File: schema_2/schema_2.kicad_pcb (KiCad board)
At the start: 2 copper layers, 241 x 211 mm, 377 parts, among them J1 USB_C_Receptacle_PowerOnly_6P, J2 Conn_01x03_Pin, J3 Conn_01x04_Pin, SW103 SW_Push, SW104 SW_Push, SW105 SW_Push, SW21 SK12D07VG3, SW92 SK12D07VG3, U1 AP2112K-3.3, U2 W25Q128JVS, U3 74AHCT125, U4 STM32G070RBTx, U5 MAX98357A, U6 WEMOS_D1_mini, Y1 SX3M8.000M20F30TNN

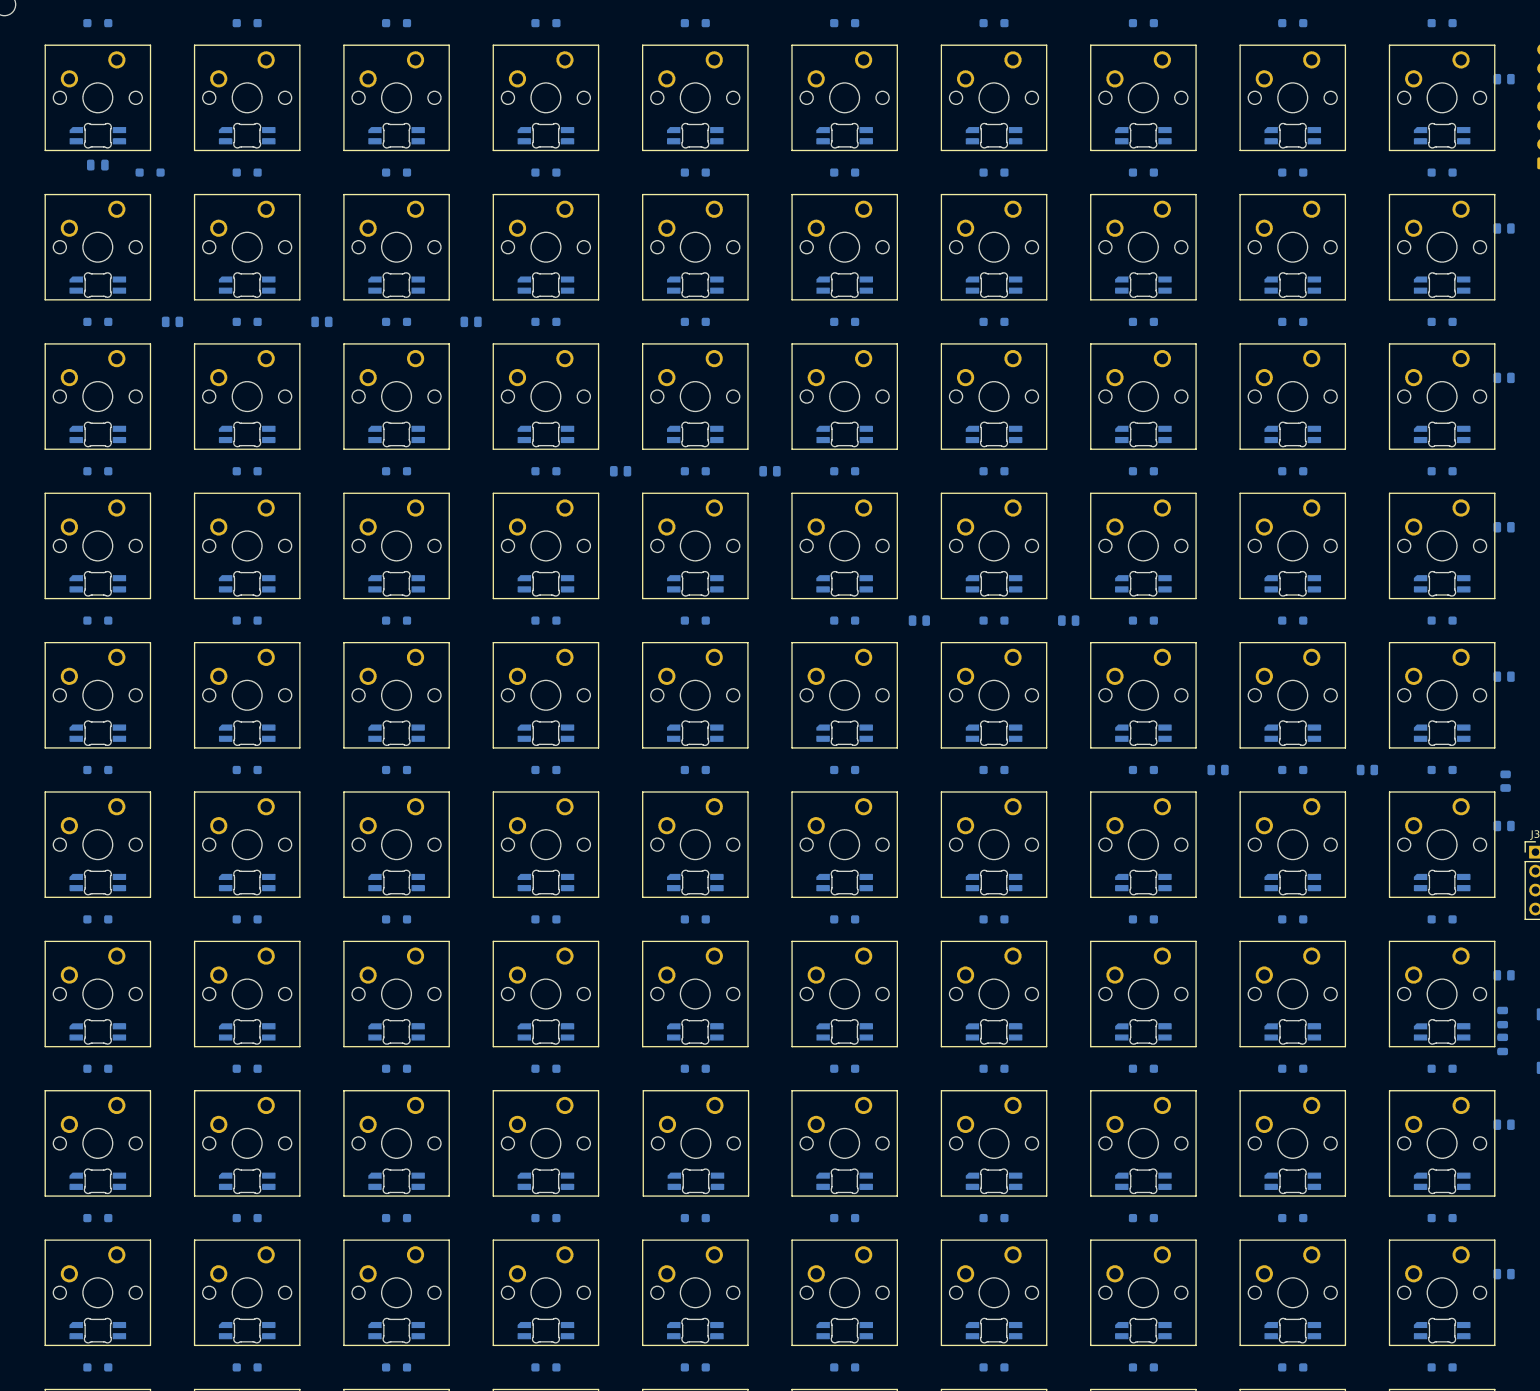
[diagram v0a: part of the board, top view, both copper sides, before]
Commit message: Update schematic and pcb with new snake connection
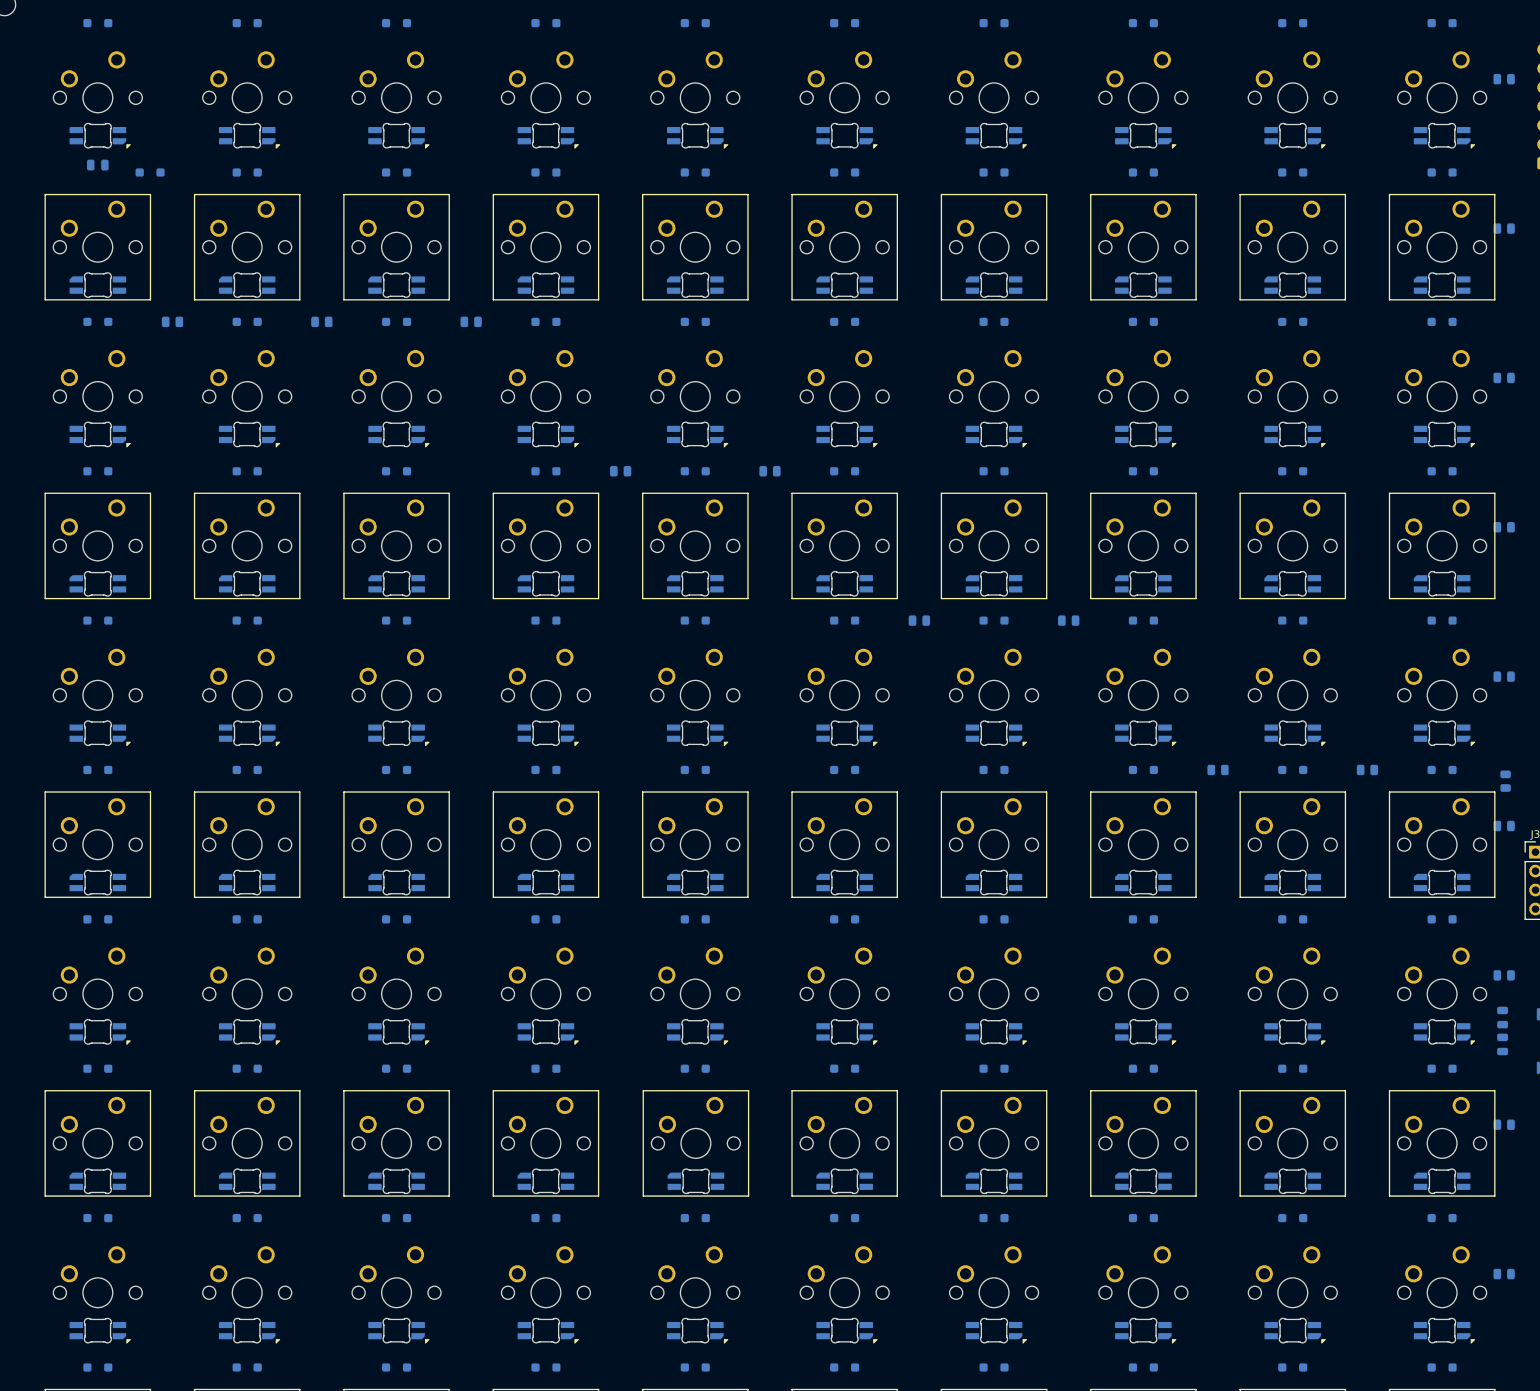
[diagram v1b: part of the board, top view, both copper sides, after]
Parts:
- SW1, SW10, SW2, SW22, SW23, SW24, SW25, SW26, SW27, SW28, SW29, SW3, SW30, SW31, SW4, SW42, SW43, SW44, SW45, SW46, SW47, SW48, SW49, SW5, SW50, SW51, SW6, SW62, SW63, SW64, SW65, SW66, SW67, SW68, SW69, SW7, SW70, SW71, SW8, SW82, SW83, SW84, SW85, SW86, SW87, SW88, SW89, SW9, SW90, SW91: footprint sw_led:SW_MX_1u_SK6812MINI-E_ROTATE -> sw_led:SW_MX_1u_SK6812MINI-E
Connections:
- net Net-(SW100-DIN) renamed /led_97
- net Net-(SW100-DOUT) renamed /led_98
- net Net-(SW101-DOUT) renamed /led_99
- net Net-(SW11-DOUT) renamed /led_11
- net Net-(SW12-DOUT) renamed /led_12
- net Net-(SW13-DOUT) renamed /led_13
- net Net-(SW14-DOUT) renamed /led_14
- net Net-(SW15-DOUT) renamed /led_15
- net Net-(SW16-DOUT) renamed /led_16
- net Net-(SW17-DOUT) renamed /led_17
- net Net-(SW18-DOUT) renamed /led_18
- net Net-(SW19-DOUT) renamed /led_19
- net Net-(SW32-DOUT) renamed /led_31
- net Net-(SW33-DOUT) renamed /led_32
- net Net-(SW34-DOUT) renamed /led_33
- net Net-(SW35-DOUT) renamed /led_34
- net Net-(SW36-DOUT) renamed /led_35
- net Net-(SW37-DOUT) renamed /led_36
- net Net-(SW38-DOUT) renamed /led_37
- net Net-(SW39-DOUT) renamed /led_38
- net Net-(SW40-DOUT) renamed /led_39
- net Net-(SW52-DOUT) renamed /led_51
- net Net-(SW53-DOUT) renamed /led_52
- net Net-(SW54-DOUT) renamed /led_53
- net Net-(SW55-DOUT) renamed /led_54
- net Net-(SW56-DOUT) renamed /led_55
- net Net-(SW57-DOUT) renamed /led_56
- net Net-(SW58-DOUT) renamed /led_57
- net Net-(SW59-DOUT) renamed /led_58
- net Net-(SW60-DOUT) renamed /led_59
- net Net-(SW72-DOUT) renamed /led_71
- net Net-(SW73-DOUT) renamed /led_72
- net Net-(SW74-DOUT) renamed /led_73
- net Net-(SW75-DOUT) renamed /led_74
- net Net-(SW76-DOUT) renamed /led_75
- net Net-(SW77-DOUT) renamed /led_76
- net Net-(SW78-DOUT) renamed /led_77
- net Net-(SW79-DOUT) renamed /led_78
- net Net-(SW80-DOUT) renamed /led_79
- net Net-(SW93-DOUT) renamed /led_91
- net Net-(SW94-DOUT) renamed /led_92
- net Net-(SW95-DOUT) renamed /led_93
- net Net-(SW96-DOUT) renamed /led_94
- net Net-(SW97-DOUT) renamed /led_95
- net Net-(SW98-DOUT) renamed /led_96
- SW1 pad 2: Net-(SW1-DOUT) -> /led_10
- SW1 pad 4: /rgb_data_5V -> /led_9
- SW10 pad 2: /led_out_1 -> /led_1
- SW10 pad 4: Net-(SW10-DIN) -> /rgb_data_5V
- SW11 pad 4: /led_out_1 -> /led_10
- SW2 pad 2: Net-(SW2-DOUT) -> /led_9
- SW2 pad 4: Net-(SW1-DOUT) -> /led_8
- SW20 pad 2: /led_out_2 -> /led_20
- SW22 pad 2: Net-(SW22-DOUT) -> /led_30
- SW22 pad 4: /led_out_2 -> /led_29
- SW23 pad 2: Net-(SW23-DOUT) -> /led_29
- SW23 pad 4: Net-(SW22-DOUT) -> /led_28
- SW24 pad 2: Net-(SW24-DOUT) -> /led_28
- SW24 pad 4: Net-(SW23-DOUT) -> /led_27
- SW25 pad 2: Net-(SW25-DOUT) -> /led_27
- SW25 pad 4: Net-(SW24-DOUT) -> /led_26
- SW26 pad 2: Net-(SW26-DOUT) -> /led_26
- SW26 pad 4: Net-(SW25-DOUT) -> /led_25
- SW27 pad 2: Net-(SW27-DOUT) -> /led_25
- SW27 pad 4: Net-(SW26-DOUT) -> /led_24
- SW28 pad 2: Net-(SW28-DOUT) -> /led_24
- SW28 pad 4: Net-(SW27-DOUT) -> /led_23
- SW29 pad 2: Net-(SW29-DOUT) -> /led_23
- SW29 pad 4: Net-(SW28-DOUT) -> /led_22
- SW3 pad 2: Net-(SW3-DOUT) -> /led_8
- SW3 pad 4: Net-(SW2-DOUT) -> /led_7
- SW30 pad 2: Net-(SW30-DOUT) -> /led_22
- SW30 pad 4: Net-(SW29-DOUT) -> /led_21
- SW31 pad 2: /led_out_3 -> /led_21
- SW31 pad 4: Net-(SW30-DOUT) -> /led_20
- SW32 pad 4: /led_out_3 -> /led_30
- SW4 pad 2: Net-(SW4-DOUT) -> /led_7
- SW4 pad 4: Net-(SW3-DOUT) -> /led_6
- SW41 pad 2: /led_out_4 -> /led_40
- SW42 pad 2: Net-(SW42-DOUT) -> /led_50
- SW42 pad 4: /led_out_4 -> /led_49
- SW43 pad 2: Net-(SW43-DOUT) -> /led_49
- SW43 pad 4: Net-(SW42-DOUT) -> /led_48
- SW44 pad 2: Net-(SW44-DOUT) -> /led_48
- SW44 pad 4: Net-(SW43-DOUT) -> /led_47
- SW45 pad 2: Net-(SW45-DOUT) -> /led_47
- SW45 pad 4: Net-(SW44-DOUT) -> /led_46
- SW46 pad 2: Net-(SW46-DOUT) -> /led_46
- SW46 pad 4: Net-(SW45-DOUT) -> /led_45
- SW47 pad 2: Net-(SW47-DOUT) -> /led_45
- SW47 pad 4: Net-(SW46-DOUT) -> /led_44
- SW48 pad 2: Net-(SW48-DOUT) -> /led_44
- SW48 pad 4: Net-(SW47-DOUT) -> /led_43
- SW49 pad 2: Net-(SW49-DOUT) -> /led_43
- SW49 pad 4: Net-(SW48-DOUT) -> /led_42
- SW5 pad 2: Net-(SW5-DOUT) -> /led_6
- SW5 pad 4: Net-(SW4-DOUT) -> /led_5
- SW50 pad 2: Net-(SW50-DOUT) -> /led_42
- SW50 pad 4: Net-(SW49-DOUT) -> /led_41
- SW51 pad 2: /led_out_5 -> /led_41
- SW51 pad 4: Net-(SW50-DOUT) -> /led_40
- SW52 pad 4: /led_out_5 -> /led_50
- SW6 pad 2: Net-(SW6-DOUT) -> /led_5
- SW6 pad 4: Net-(SW5-DOUT) -> /led_4
- SW61 pad 2: /led_out_6 -> /led_60
- SW62 pad 2: Net-(SW62-DOUT) -> /led_70
- SW62 pad 4: /led_out_6 -> /led_69
- SW63 pad 2: Net-(SW63-DOUT) -> /led_69
- SW63 pad 4: Net-(SW62-DOUT) -> /led_68
- SW64 pad 2: Net-(SW64-DOUT) -> /led_68
- SW64 pad 4: Net-(SW63-DOUT) -> /led_67
- SW65 pad 2: Net-(SW65-DOUT) -> /led_67
- SW65 pad 4: Net-(SW64-DOUT) -> /led_66
- SW66 pad 2: Net-(SW66-DOUT) -> /led_66
- SW66 pad 4: Net-(SW65-DOUT) -> /led_65
- SW67 pad 2: Net-(SW67-DOUT) -> /led_65
- SW67 pad 4: Net-(SW66-DOUT) -> /led_64
- SW68 pad 2: Net-(SW68-DOUT) -> /led_64
- SW68 pad 4: Net-(SW67-DOUT) -> /led_63
- SW69 pad 2: Net-(SW69-DOUT) -> /led_63
- SW69 pad 4: Net-(SW68-DOUT) -> /led_62
- SW7 pad 2: Net-(SW7-DOUT) -> /led_4
- SW7 pad 4: Net-(SW6-DOUT) -> /led_3
- SW70 pad 2: Net-(SW70-DOUT) -> /led_62
- SW70 pad 4: Net-(SW69-DOUT) -> /led_61
- SW71 pad 2: /led_out_7 -> /led_61
- SW71 pad 4: Net-(SW70-DOUT) -> /led_60
- SW72 pad 4: /led_out_7 -> /led_70
- SW8 pad 2: Net-(SW8-DOUT) -> /led_3
- SW8 pad 4: Net-(SW7-DOUT) -> /led_2
- SW81 pad 2: /led_out_8 -> /led_80
- SW82 pad 2: Net-(SW82-DOUT) -> /led_90
- SW82 pad 4: /led_out_8 -> /led_89
- SW83 pad 2: Net-(SW83-DOUT) -> /led_89
- SW83 pad 4: Net-(SW82-DOUT) -> /led_88
- SW84 pad 2: Net-(SW84-DOUT) -> /led_88
- SW84 pad 4: Net-(SW83-DOUT) -> /led_87
- SW85 pad 2: Net-(SW85-DOUT) -> /led_87
- SW85 pad 4: Net-(SW84-DOUT) -> /led_86
- SW86 pad 2: Net-(SW86-DOUT) -> /led_86
- SW86 pad 4: Net-(SW85-DOUT) -> /led_85
- SW87 pad 2: Net-(SW87-DOUT) -> /led_85
- SW87 pad 4: Net-(SW86-DOUT) -> /led_84
- SW88 pad 2: Net-(SW88-DOUT) -> /led_84
- SW88 pad 4: Net-(SW87-DOUT) -> /led_83
- SW89 pad 2: Net-(SW89-DOUT) -> /led_83
- SW89 pad 4: Net-(SW88-DOUT) -> /led_82
- SW9 pad 2: Net-(SW10-DIN) -> /led_2
- SW9 pad 4: Net-(SW8-DOUT) -> /led_1
- SW90 pad 2: Net-(SW90-DOUT) -> /led_82
- SW90 pad 4: Net-(SW89-DOUT) -> /led_81
- SW91 pad 2: /led_out_9 -> /led_81
- SW91 pad 4: Net-(SW90-DOUT) -> /led_80
- SW93 pad 4: /led_out_9 -> /led_90
